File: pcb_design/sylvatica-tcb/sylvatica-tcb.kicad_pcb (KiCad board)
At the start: 2 copper layers, 93 x 93 mm, 6 parts, among them J1 Conn_02x07_Odd_Even, J2 USB_C_Receptacle, J3 USB_C_Receptacle, J4 USB_C_Receptacle, J5 USB_C_Receptacle

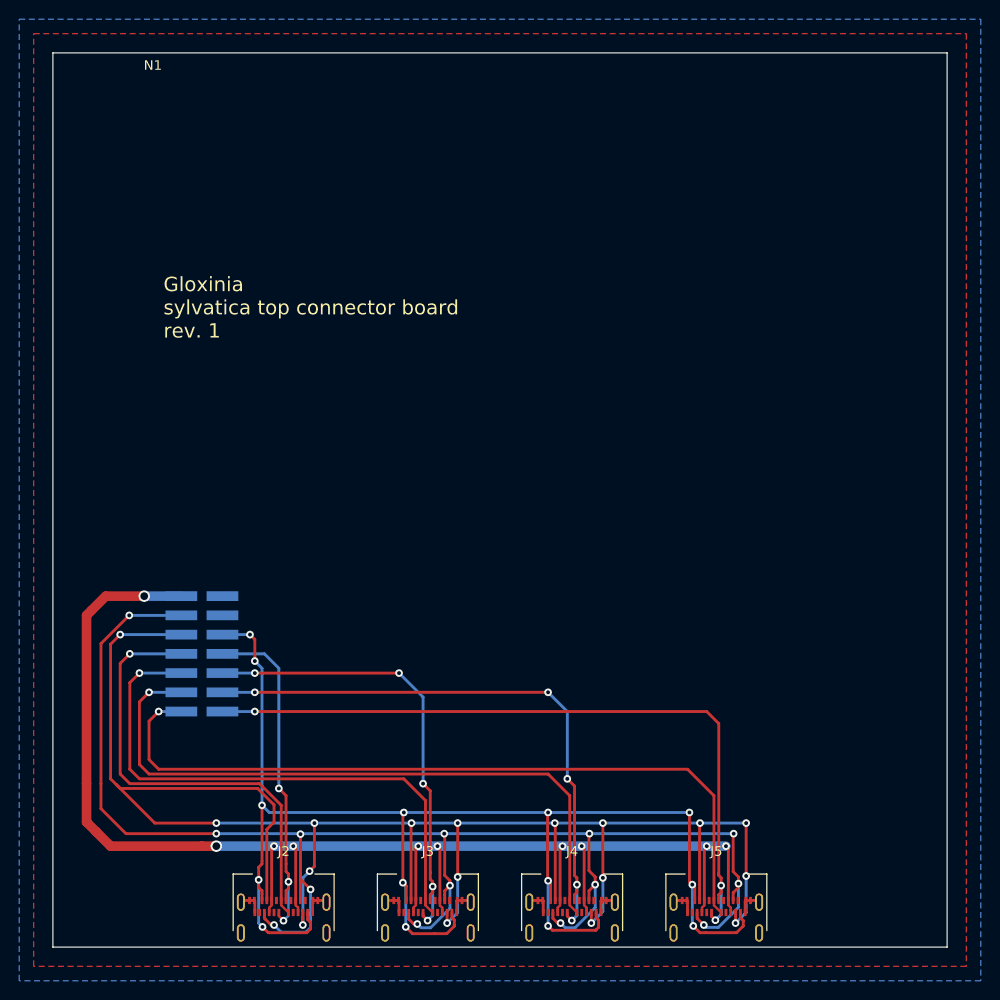
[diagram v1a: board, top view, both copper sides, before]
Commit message: Bug fix in component layout
Connector was not updated to latest version, resulting in mis alignment w.r.t. connector board.
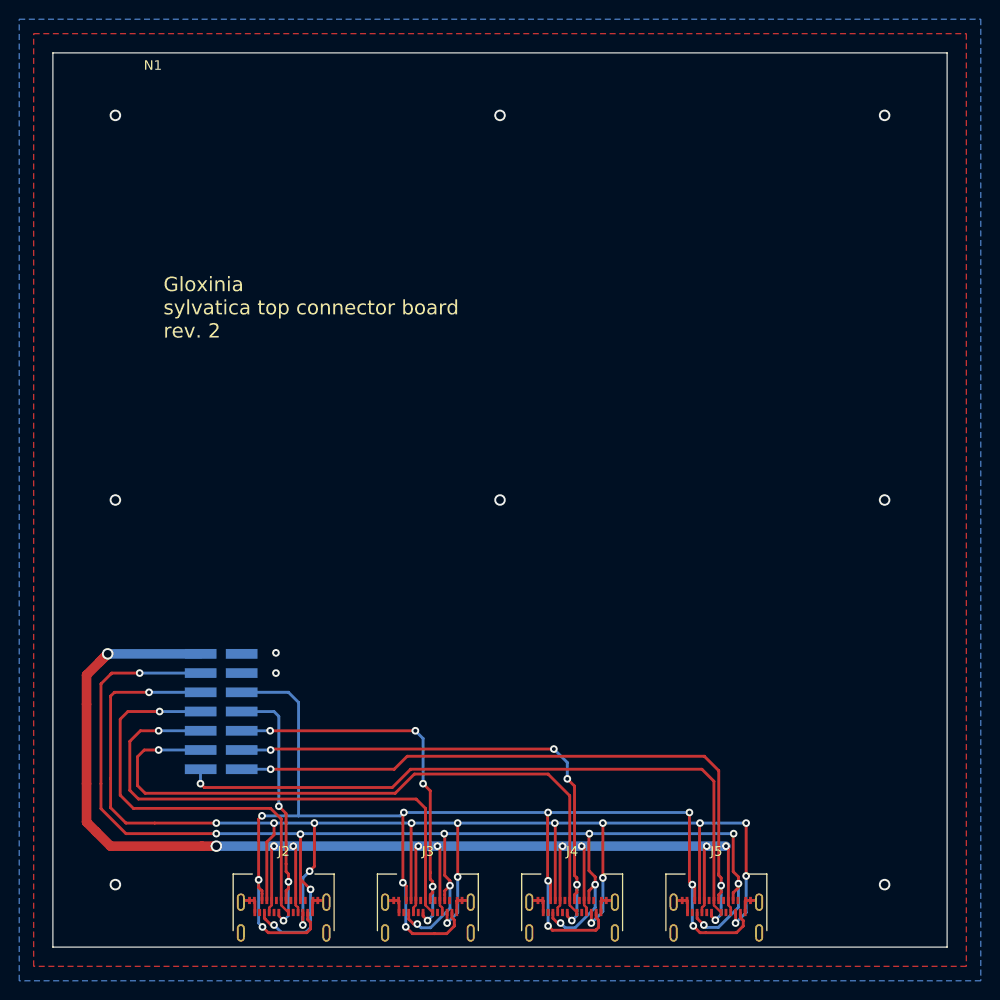
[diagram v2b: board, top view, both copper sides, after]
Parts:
- moved J1 6.32 mm to (56.0, 107.0)
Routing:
- net /SDA2: track 189.8 -> 168.8 mm, vias 17 -> 18
- net /OW8: track 80.5 -> 70.3 mm
- net /EV5: track 36.5 -> 29.1 mm
- net /EV7: track 61.9 -> 54.4 mm
- net /EV6: track 48.4 -> 41.4 mm
- net /EV8: track 75.6 -> 69.3 mm
- net /~{INT2}: track 151.9 -> 147.6 mm, vias 14 -> 12
- net /OW5: track 47.8 -> 44.4 mm
- net /OW6: track 58.8 -> 55.6 mm
- net /SCL2: track 161.0 -> 158.0 mm
- net /S_PS2: track 156.6 -> 153.7 mm
- net GND: vias 0 -> 10
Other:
- board text added: "Gloxinia sylvatica top connector board rev. 2"
- board text removed: "Gloxinia sylvatica top connector board rev. 1"

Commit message: Various updates for Aisler order.
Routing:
- net /S_PS2: track 153.7 -> 152.5 mm
